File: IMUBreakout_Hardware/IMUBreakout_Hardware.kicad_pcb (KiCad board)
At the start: 2 copper layers, 30.5 x 25.4 mm, 11 parts, among them U1 LSM90S1

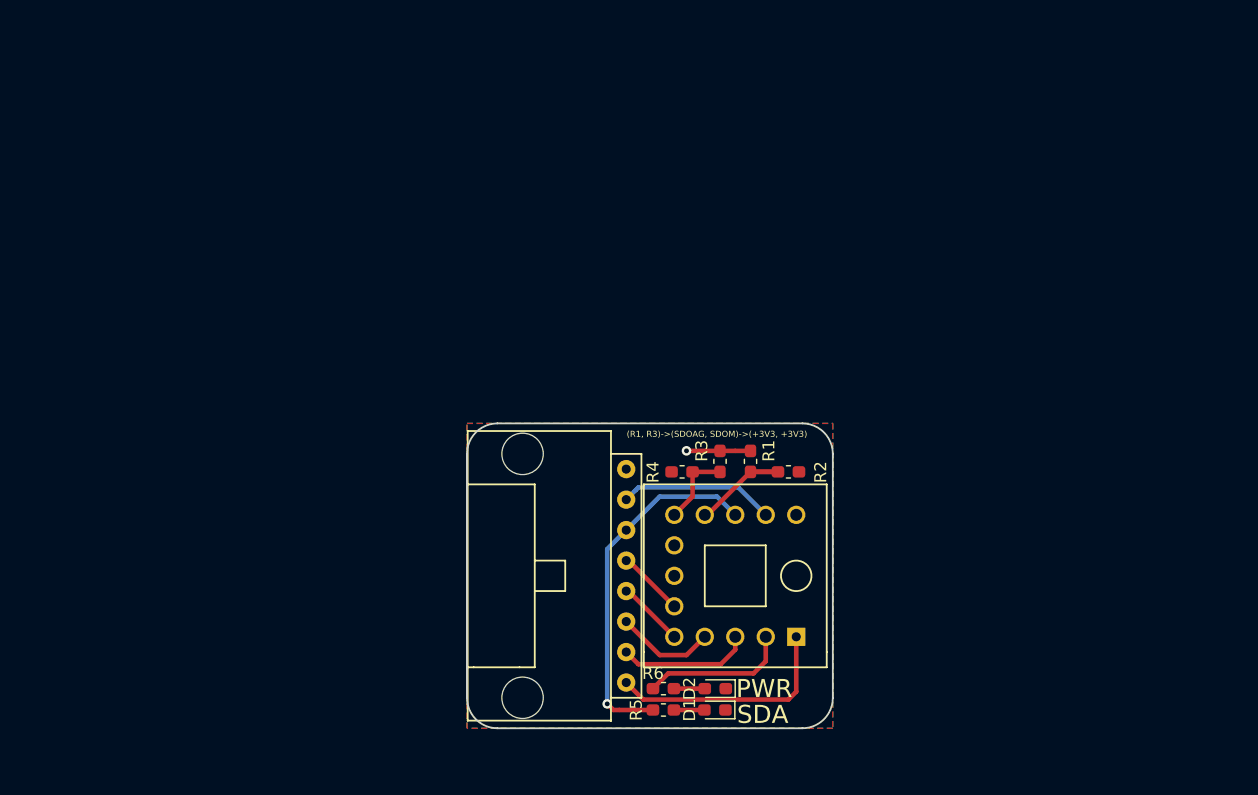
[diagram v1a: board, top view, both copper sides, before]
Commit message: Schematic and PCB created
Rough outlines of board
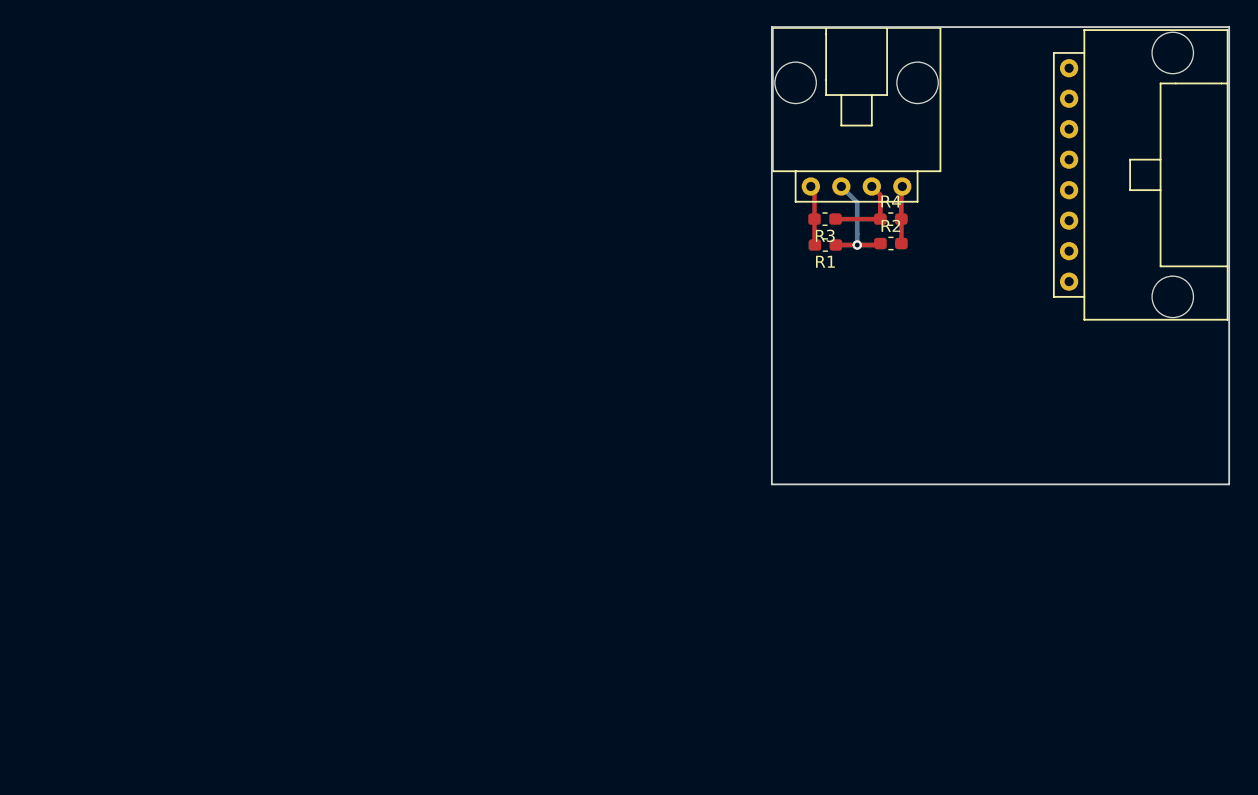
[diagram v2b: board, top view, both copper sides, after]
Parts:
- removed D1, D2: D, Diode_SMD:D_0603_1608Metric_Pad1.05x0.95mm_HandSolder
- removed G***: LOGO, MRDT_Silkscreens:MRDT_Logo_10mm
- removed R5, R6: 500, Resistor_SMD:R_0603_1608Metric_Pad1.05x0.95mm_HandSolder
- removed U1: LSM90S1, MRDT_Sensors:IMU_LSM90S1
- added Conn2: Molex_SL_08, MRDT_Connectors:MOLEX_SL_08_Horizontal, F.Cu at (184.8, 65.7)
- Conn1: value Molex_SL_08 -> Molex_SL_04; footprint MRDT_Connectors:MOLEX_SL_08_Horizontal -> MRDT_Connectors:MOLEX_SL_04_Horizontal
- R1, R3: value 0 -> 500
- R2, R4: value 1K -> 500
- moved Conn1 37.7 mm to (167.1, 66.6), turned to 0 degrees
- moved R4 27.3 mm to (169.9, 69.3), turned to 0 degrees
- moved R3 22.0 mm to (164.5, 69.3), turned to 180 degrees
- moved R2 20.9 mm to (169.9, 71.4)
- moved R1 19.1 mm to (164.5, 71.5), turned to 180 degrees
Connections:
- Conn1 pad 1: GND -> +3V3
- Conn1 pad 2: INT2AG -> TX
- Conn1 pad 3: INT1AG -> RX
- Conn1 pad 4: INTM -> GND
- R1 pad 1: SDOAG -> TX
- R2 pad 1: SDOAG -> TX
- R3 pad 1: SDOM -> RX
- R4 pad 1: SDOM -> RX
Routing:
- net SDA: track 30.0 -> 0.00 mm, vias 1 -> 0
- net GND: track 19.6 -> 4.80 mm
- net SCL: track 13.0 -> 0.00 mm
- net +3V3: track 17.7 -> 5.17 mm, vias 1 -> 0
- net INT2AG: track 11.1 -> 0.00 mm
- net SDOAG: track 9.61 -> 0.00 mm
- net TX: track 0.00 -> 9.19 mm, vias 0 -> 1
- net INT1AG: track 8.33 -> 0.00 mm
- net RX: track 0.00 -> 6.73 mm
- net SDOM: track 6.50 -> 0.00 mm
- net INTM: track 5.39 -> 0.00 mm
- net DRDYM: track 5.39 -> 0.00 mm
- net Net-(D2-Pad2): track 2.54 -> 0.00 mm
- net Net-(D1-Pad2): track 2.54 -> 0.00 mm
- removed copper zone on B.Cu, net +3V3
- removed copper zone on F.Cu, net GND
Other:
- board size 30.5 x 25.4 mm -> 38.1 x 38.1 mm
- board text removed: "(R1, R3)->(SDOAG, SDOM)->(+3V3, +3V3)"
- board text removed: "IMU Breakout, Rev 1 Mars Rover, 2019 Missouri S&T"
- board text removed: "PWR"
- board text removed: "SDA"

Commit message: SilkScreens
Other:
- board text added: "LEDs"
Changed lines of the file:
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@@
   (general
     (thickness 1.6)
-    (drawings 6)
+    (drawings 12)
     (tracks 21)
     (zones 0)
@@
       (net 12 "Net-(Conn2-Pad8)"))
   )
+  (gr_text "LEDs\n" (at 167.513 74.93) (layer F.SilkS)
+    (effects (font (size 1.5 1.5) (thickness 0.3)))
+  )
+  (gr_line (start 162.179 73.533) (end 162.433 73.533) (layer F.SilkS) (width 0.2))
+  (gr_line (start 162.179 68.326) (end 162.179 73.533) (layer F.SilkS) (width 0.2))
+  (gr_line (start 172.593 73.533) (end 162.433 73.533) (layer F.SilkS) (width 0.2))
+  (gr_line (start 172.593 68.326) (end 172.593 73.533) (layer F.SilkS) (width 0.2))
+  (gr_line (start 162.179 68.326) (end 172.593 68.326) (layer F.SilkS) (width 0.2))
   (gr_line (start 160.02 91.44) (end 160.02 53.34) (layer Edge.Cuts) (width 0.15))
   (gr_line (start 198.12 91.44) (end 160.02 91.44) (layer Edge.Cuts) (width 0.15))

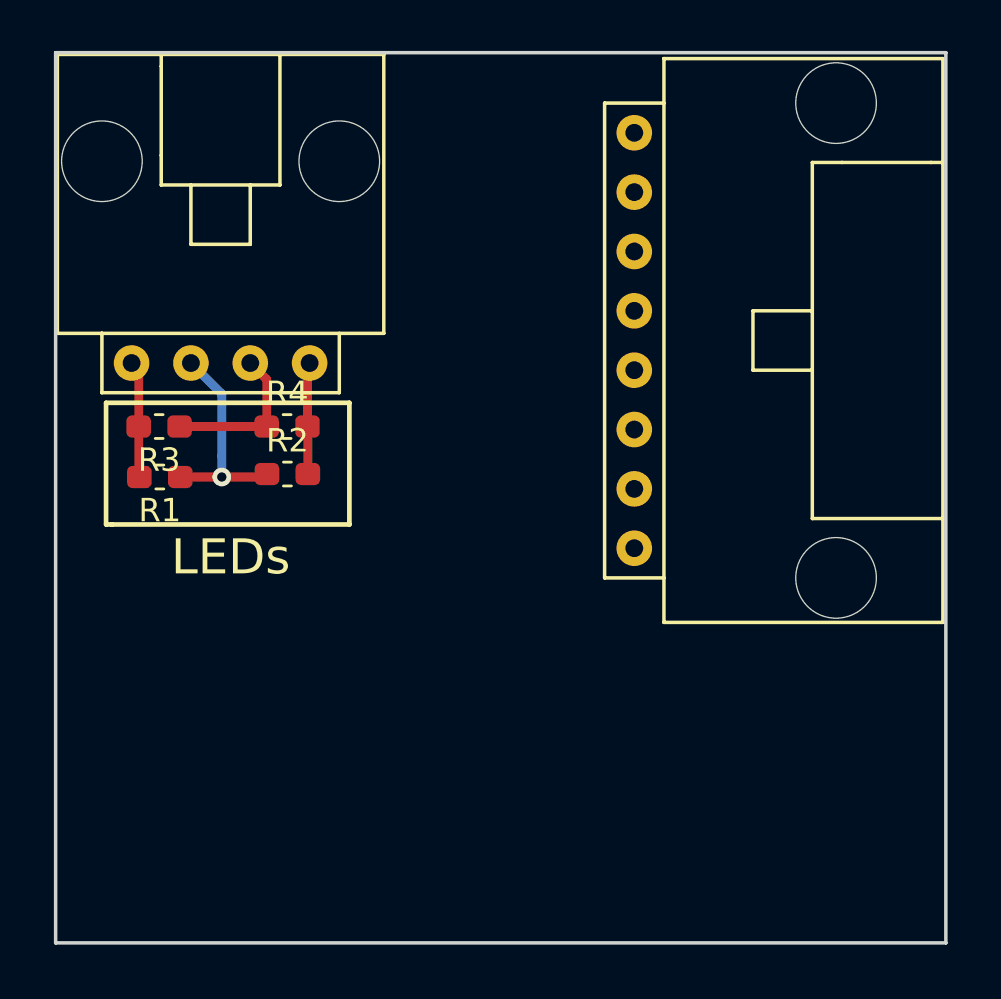
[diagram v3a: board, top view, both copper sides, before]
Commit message: Changed Board based on Andrew's notes
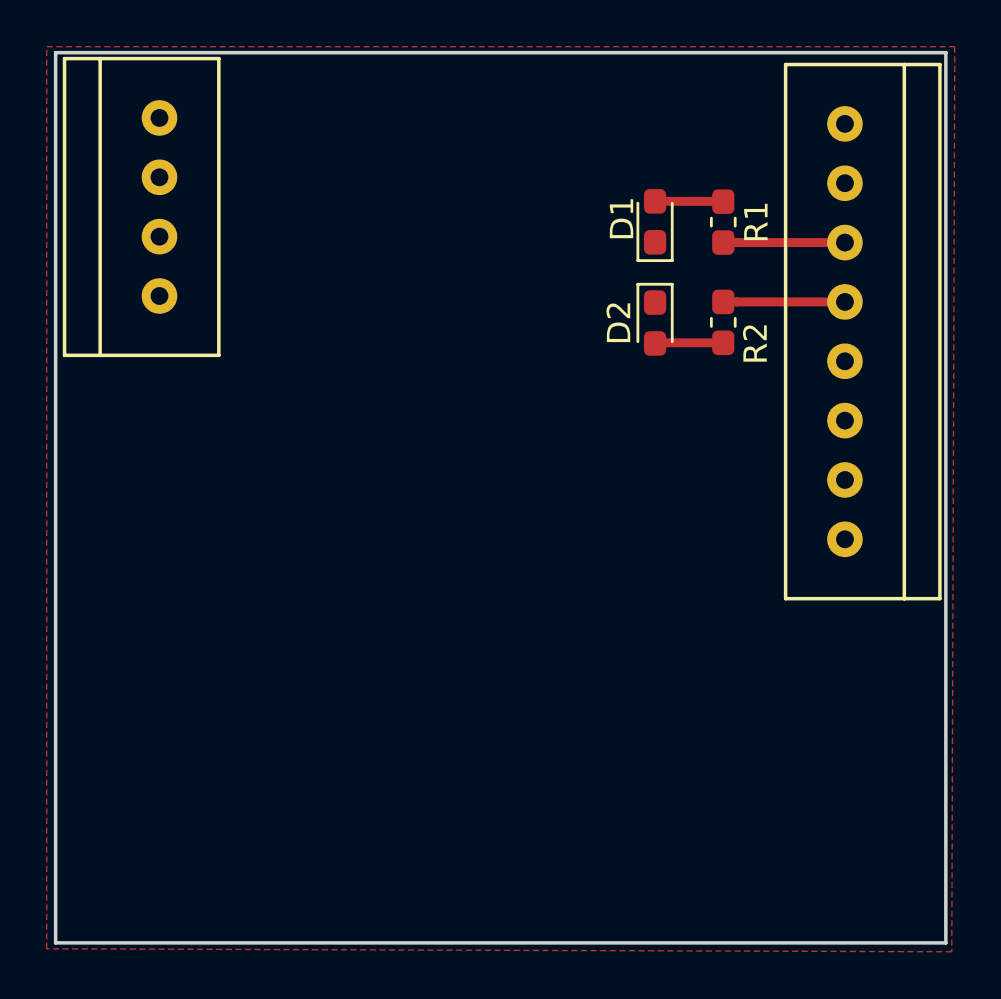
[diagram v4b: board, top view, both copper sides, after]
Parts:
- removed R3, R4: 500, Resistor_SMD:R_0603_1608Metric_Pad1.05x0.95mm_HandSolder
- added D1: LED, LED_SMD:LED_0603_1608Metric_Pad1.05x0.95mm_HandSolder, F.Cu at (185.7, 60.6)
- added D2: LED, LED_SMD:LED_0603_1608Metric_Pad1.05x0.95mm_HandSolder, F.Cu at (185.7, 64.9)
- Conn1: footprint MRDT_Connectors:MOLEX_SL_04_Horizontal -> MRDT_Connectors:MOLEX_SL_04_Vertical
- Conn2: footprint MRDT_Connectors:MOLEX_SL_08_Horizontal -> MRDT_Connectors:MOLEX_SL_08_Vertical
- moved R1 26.5 mm to (188.6, 60.6), turned to 270 degrees
- moved R2 19.8 mm to (188.6, 64.9), turned to 90 degrees
- moved Conn2 9.03 mm to (193.8, 65.3)
- moved Conn1 7.17 mm to (164.5, 59.9), turned to 90 degrees
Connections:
- Conn1 pad 1: +3V3 -> Net-(Conn1-Pad1)
- Conn1 pad 2: TX -> Net-(Conn1-Pad2)
- Conn1 pad 3: RX -> Net-(Conn1-Pad3)
- Conn1 pad 4: GND -> Net-(Conn1-Pad4)
- Conn2 pad 1: Net-(Conn2-Pad1) -> GND
- Conn2 pad 2: Net-(Conn2-Pad2) -> +3V3
- Conn2 pad 3: Net-(Conn2-Pad3) -> RX
- Conn2 pad 4: Net-(Conn2-Pad4) -> TX
- R1 pad 1: TX -> Net-(D1-Pad2)
- R1 pad 2: +3V3 -> RX
- R2 pad 1: TX -> Net-(D2-Pad2)
- R2 pad 2: GND -> TX
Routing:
- net +3V3: track 5.17 -> 0.00 mm
- net GND: track 4.80 -> 0.00 mm
- net TX: track 9.19 -> 5.21 mm, vias 1 -> 0
- net Net-(D2-Pad2): track 0.00 -> 2.93 mm
- net Net-(D1-Pad2): track 0.00 -> 2.93 mm
- net RX: track 6.73 -> 5.21 mm
- added copper zone on F.Cu, net GND
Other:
- board text removed: "LEDs"

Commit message: created new part
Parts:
- removed Conn2: Molex_SL_08, MRDT_Connectors:MOLEX_SL_08_Vertical
- added U1: Razor_9DOF_Sparkfun, MRDT_Sensors:Razor_9DOF_Sparkfun, F.Cu at (97.8, 87.6)
- Conn1: footprint MRDT_Connectors:MOLEX_SL_04_Vertical -> MRDT_Connectors:MOLEX_SL_04_Horizontal
- moved R1 91.4 mm to (115.0, 114.8), turned to 0 degrees
- moved D1 88.1 mm to (115.1, 113.2), turned to 0 degrees
- moved R2 69.1 mm to (129.1, 100.1), turned to 0 degrees
- moved D2 65.8 mm to (129.2, 98.6), turned to 0 degrees
- moved Conn1 59.0 mm to (113.0, 88.9), turned to 180 degrees
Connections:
- Conn1 pad 1: Net-(Conn1-Pad1) -> GND
- Conn1 pad 2: Net-(Conn1-Pad2) -> +3V3
- Conn1 pad 3: Net-(Conn1-Pad3) -> RX
- Conn1 pad 4: Net-(Conn1-Pad4) -> TX
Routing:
- net TX: track 5.21 -> 0.00 mm
- net RX: track 5.21 -> 0.00 mm
- net Net-(D2-Pad2): track 2.93 -> 0.00 mm
- net Net-(D1-Pad2): track 2.93 -> 0.00 mm
- removed copper zone on F.Cu, net GND
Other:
- board outline removed

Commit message: PCB Finalzied and Made
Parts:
- moved D1 59.2 mm to (160.8, 75.6)
- moved R1 58.9 mm to (160.8, 77.7), turned to 180 degrees
- moved Conn1 49.0 mm to (161.3, 80.5)
- moved U1 48.1 mm to (145.5, 93.8)
- moved D2 35.7 mm to (156.6, 75.7), turned to 180 degrees
- moved R2 35.4 mm to (156.6, 77.8)
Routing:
- net +3V3: track 0.00 -> 32.8 mm
- net TX: track 0.00 -> 21.8 mm
- net RX: track 0.00 -> 19.3 mm
- net Net-(D1-Pad2): track 0.00 -> 2.32 mm
- net Net-(D2-Pad2): track 0.00 -> 2.09 mm
- added copper zone on F.Cu, net GND
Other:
- board outline added: 31.8 x 31.8 mm
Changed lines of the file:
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@@
-(kicad_pcb (version 20171130) (host pcbnew "(5.0.2)-1")
+(kicad_pcb (version 20171130) (host pcbnew "(5.0.0)")
   (general
     (thickness 1.6)
-    (drawings 2)
-    (tracks 0)
+    (drawings 10)
+    (tracks 19)
     (zones 0)
     (modules 6)
@@
   )
   (setup
-    (last_trace_width 0.25)
+    (last_trace_width 0.381)
     (user_trace_width 0.381)
     (trace_clearance 0.2)
@@
   )
   (module MRDT_Connectors:MOLEX_SL_04_Horizontal (layer F.Cu)
-    (at 113.03 88.9 180)
-    (fp_text reference Conn1 (at -2.54 2.54 180) (layer F.SilkS) hide
+    (at 161.29 80.518 180)
+    (fp_text reference Conn1 (at -4.572 -2.032 180) (layer F.SilkS) hide
       (effects (font (size 1 1) (thickness 0.15)))
     )
@@
   )
   (module LED_SMD:LED_0603_1608Metric_Pad1.05x0.95mm_HandSolder (layer F.Cu)
-    (at 115.070001 113.205001)
+    (at 160.785626 75.55623)
     (descr "LED SMD 0603 (1608 Metric), square (rectangular) end terminal, IPC_7351 nominal, (Body size source: http://www.tortai-tech.com/upload/download/2011102023233369053.pdf), generated with kicad-footprint-generator")
     (tags "LED handsolder")
     (attr smd)
-    (fp_text reference D1 (at 0 -1.43) (layer F.SilkS)
+    (fp_text reference D1 (at 2.790374 -0.11823) (layer F.SilkS)
       (effects (font (size 1 1) (thickness 0.15)))
     )
@@
   )
   (module LED_SMD:LED_0603_1608Metric_Pad1.05x0.95mm_HandSolder (layer F.Cu)
-    (at 129.190001 98.585001)
+    (at 156.577 75.692 180)
     (descr "LED SMD 0603 (1608 Metric), square (rectangular) end terminal, IPC_7351 nominal, (Body size source: http://www.tortai-tech.com/upload/download/2011102023233369053.pdf), generated with kicad-footprint-generator")
     (tags "LED handsolder")
     (attr smd)
-    (fp_text reference D2 (at 0 -1.43) (layer F.SilkS)
-      (effects (font (size 1 1) (thickness 0.15)))
-    )
-    (fp_text value LED (at 0 1.43) (layer F.Fab)
+    (fp_text reference D2 (at 2.907 0 180) (layer F.SilkS)
+      (effects (font (size 1 1) (thickness 0.15)))
+    )
+    (fp_text value LED (at 0 1.43 180) (layer F.Fab)
       (effects (font (size 1 1) (thickness 0.15)))
     )
@@
     (fp_line (start 1.65 -0.73) (end 1.65 0.73) (layer F.CrtYd) (width 0.05))
     (fp_line (start 1.65 0.73) (end -1.65 0.73) (layer F.CrtYd) (width 0.05))
-    (fp_text user %R (at 0 0) (layer F.Fab)
+    (fp_text user %R (at 0 0 180) (layer F.Fab)
       (effects (font (size 0.4 0.4) (thickness 0.06)))
     )
-    (pad 1 smd roundrect (at -0.875 0) (size 1.05 0.95) (layers F.Cu F.Paste F.Mask) (roundrect_rratio 0.25)
+    (pad 1 smd roundrect (at -0.875 0 180) (size 1.05 0.95) (layers F.Cu F.Paste F.Mask) (roundrect_rratio 0.25)
       (net 1 GND))
-    (pad 2 smd roundrect (at 0.875 0) (size 1.05 0.95) (layers F.Cu F.Paste F.Mask) (roundrect_rratio 0.25)
+    (pad 2 smd roundrect (at 0.875 0 180) (size 1.05 0.95) (layers F.Cu F.Paste F.Mask) (roundrect_rratio 0.25)
       (net 6 "Net-(D2-Pad2)"))
     (model ${KISYS3DMOD}/LED_SMD.3dshapes/LED_0603_1608Metric.wrl
@@
   )
   (module Resistor_SMD:R_0603_1608Metric_Pad1.05x0.95mm_HandSolder (layer F.Cu)
-    (at 115.025001 114.755001)
+    (at 160.782 77.724 180)
     (descr "Resistor SMD 0603 (1608 Metric), square (rectangular) end terminal, IPC_7351 nominal with elongated pad for handsoldering. (Body size source: http://www.tortai-tech.com/upload/download/2011102023233369053.pdf), generated with kicad-footprint-generator")
     (tags "resistor handsolder")
     (attr smd)
-    (fp_text reference R1 (at 0 -1.43) (layer F.SilkS)
-      (effects (font (size 1 1) (thickness 0.15)))
-    )
-    (fp_text value 500 (at 0 1.43) (layer F.Fab)
-      (effects (font (size 1 1) (thickness 0.15)))
-    )
-    (fp_text user %R (at 0 0) (layer F.Fab)
+    (fp_text reference R1 (at -2.794 0 180) (layer F.SilkS)
+      (effects (font (size 1 1) (thickness 0.15)))
+    )
+    (fp_text value 500 (at 0 1.43 180) (layer F.Fab)
+      (effects (font (size 1 1) (thickness 0.15)))
+    )
+    (fp_text user %R (at 0 0 180) (layer F.Fab)
       (effects (font (size 0.4 0.4) (thickness 0.06)))
     )
@@
     (fp_line (start -0.8 -0.4) (end 0.8 -0.4) (layer F.Fab) (width 0.1))
     (fp_line (start -0.8 0.4) (end -0.8 -0.4) (layer F.Fab) (width 0.1))
-    (pad 2 smd roundrect (at 0.875 0) (size 1.05 0.95) (layers F.Cu F.Paste F.Mask) (roundrect_rratio 0.25)
+    (pad 2 smd roundrect (at 0.875 0 180) (size 1.05 0.95) (layers F.Cu F.Paste F.Mask) (roundrect_rratio 0.25)
       (net 4 RX))
-    (pad 1 smd roundrect (at -0.875 0) (size 1.05 0.95) (layers F.Cu F.Paste F.Mask) (roundrect_rratio 0.25)
+    (pad 1 smd roundrect (at -0.875 0 180) (size 1.05 0.95) (layers F.Cu F.Paste F.Mask) (roundrect_rratio 0.25)
       (net 5 "Net-(D1-Pad2)"))
     (model ${KISYS3DMOD}/Resistor_SMD.3dshapes/R_0603_1608Metric.wrl
@@
   )
   (module Resistor_SMD:R_0603_1608Metric_Pad1.05x0.95mm_HandSolder (layer F.Cu)
-    (at 129.145001 100.135001)
+    (at 156.577001 77.783001)
     (descr "Resistor SMD 0603 (1608 Metric), square (rectangular) end terminal, IPC_7351 nominal with elongated pad for handsoldering. (Body size source: http://www.tortai-tech.com/upload/download/2011102023233369053.pdf), generated with kicad-footprint-generator")
     (tags "resistor handsolder")
     (attr smd)
-    (fp_text reference R2 (at 0 -1.43) (layer F.SilkS)
+    (fp_text reference R2 (at -2.653001 -0.059001) (layer F.SilkS)
       (effects (font (size 1 1) (thickness 0.15)))
     )
@@
   )
   (module MRDT_Sensors:Razor_9DOF_Sparkfun (layer F.Cu)
-    (at 97.79 87.63)
+    (at 145.538 93.808185)
     (fp_text reference U1 (at 5.08 1.143) (layer F.SilkS)
       (effects (font (size 1 1) (thickness 0.15)))
@@
       (net 1 GND))
   )
+  (gr_line (start 148.082 62.0395) (end 174.752 62.0395) (layer Edge.Cuts) (width 0.15))
+  (gr_line (start 148.0185 93.853) (end 174.879 93.7895) (layer Edge.Cuts) (width 0.15))
+  (gr_arc (start 148.082 64.5795) (end 148.209 62.0395) (angle -97.04732902) (layer Edge.Cuts) (width 0.15))
+  (gr_arc (start 148.082 91.313) (end 145.542 91.313) (angle -90) (layer Edge.Cuts) (width 0.15))
+  (gr_arc (start 174.752 91.2495) (end 174.752 93.7895) (angle -90) (layer Edge.Cuts) (width 0.15))
+  (gr_line (start 177.292 64.5795) (end 177.292 91.3765) (layer Edge.Cuts) (width 0.15))
+  (gr_arc (start 174.752 64.5795) (end 177.292 64.5795) (angle -90) (layer Edge.Cuts) (width 0.15))
+  (gr_line (start 145.542 64.516) (end 145.542 91.2495) (layer Edge.Cuts) (width 0.15))
   (dimension 25.4 (width 0.3) (layer F.Fab)
     (gr_text "1.0000 in" (at 107.12 99.06 90) (layer F.Fab)
@@
     (arrow2b (pts (xy 134.62 127) (xy 135.746504 126.413579)))
   )
+  (segment (start 158.801999 84.276001) (end 146.808 84.276001) (width 0.381) (layer F.Cu) (net 2))
+  (segment (start 161.341999 84.276001) (end 158.801999 84.276001) (width 0.381) (layer F.Cu) (net 2))
+  (segment (start 162.56 80.518) (end 162.56 83.058) (width 0.381) (layer F.Cu) (net 2))
+  (segment (start 162.56 83.058) (end 161.341999 84.276001) (width 0.381) (layer F.Cu) (net 2))
+  (segment (start 163.778001 84.276001) (end 162.56 83.058) (width 0.381) (layer F.Cu) (net 2))
+  (segment (start 176.017999 84.276001) (end 163.778001 84.276001) (width 0.381) (layer F.Cu) (net 2))
+  (segment (start 157.48 77.811) (end 157.452001 77.783001) (width 0.381) (layer F.Cu) (net 3))
+  (segment (start 157.48 80.518) (end 157.48 77.811) (width 0.381) (layer F.Cu) (net 3))
+  (segment (start 158.801999 79.196001) (end 176.017999 79.196001) (width 0.381) (layer B.Cu) (net 3))
+  (segment (start 157.48 80.518) (end 158.801999 79.196001) (width 0.381) (layer B.Cu) (net 3))
+  (segment (start 160.02 77.837) (end 159.907 77.724) (width 0.381) (layer F.Cu) (net 4))
+  (segment (start 160.02 80.518) (end 160.02 77.837) (width 0.381) (layer F.Cu) (net 4))
+  (segment (start 161.238001 81.736001) (end 160.02 80.518) (width 0.381) (layer B.Cu) (net 4))
+  (segment (start 176.017999 81.736001) (end 161.238001 81.736001) (width 0.381) (layer B.Cu) (net 4))
+  (segment (start 161.556625 75.660231) (end 161.660626 75.55623) (width 0.381) (layer F.Cu) (net 5))
+  (segment (start 161.660626 77.720374) (end 161.657 77.724) (width 0.381) (layer F.Cu) (net 5))
+  (segment (start 161.660626 75.55623) (end 161.660626 77.720374) (width 0.381) (layer F.Cu) (net 5))
+  (segment (start 155.702 77.783) (end 155.702001 77.783001) (width 0.381) (layer F.Cu) (net 6))
+  (segment (start 155.702 75.692) (end 155.702 77.783) (width 0.381) (layer F.Cu) (net 6))
+  (zone (net 1) (net_name GND) (layer F.Cu) (hatch edge 0.508)
+    (connect_pads (clearance 0.508))
+    (min_thickness 0.254)
+    (fill yes (arc_segments 16) (thermal_gap 0.508) (thermal_bridge_width 0.508))
+    (polygon
+      (pts
+        (xy 144.78 60.96) (xy 177.8 60.96) (xy 177.8 93.98) (xy 144.78 93.98)
+      )
+    )
+  )
 )
